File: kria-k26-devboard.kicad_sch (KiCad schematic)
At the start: 6 parts

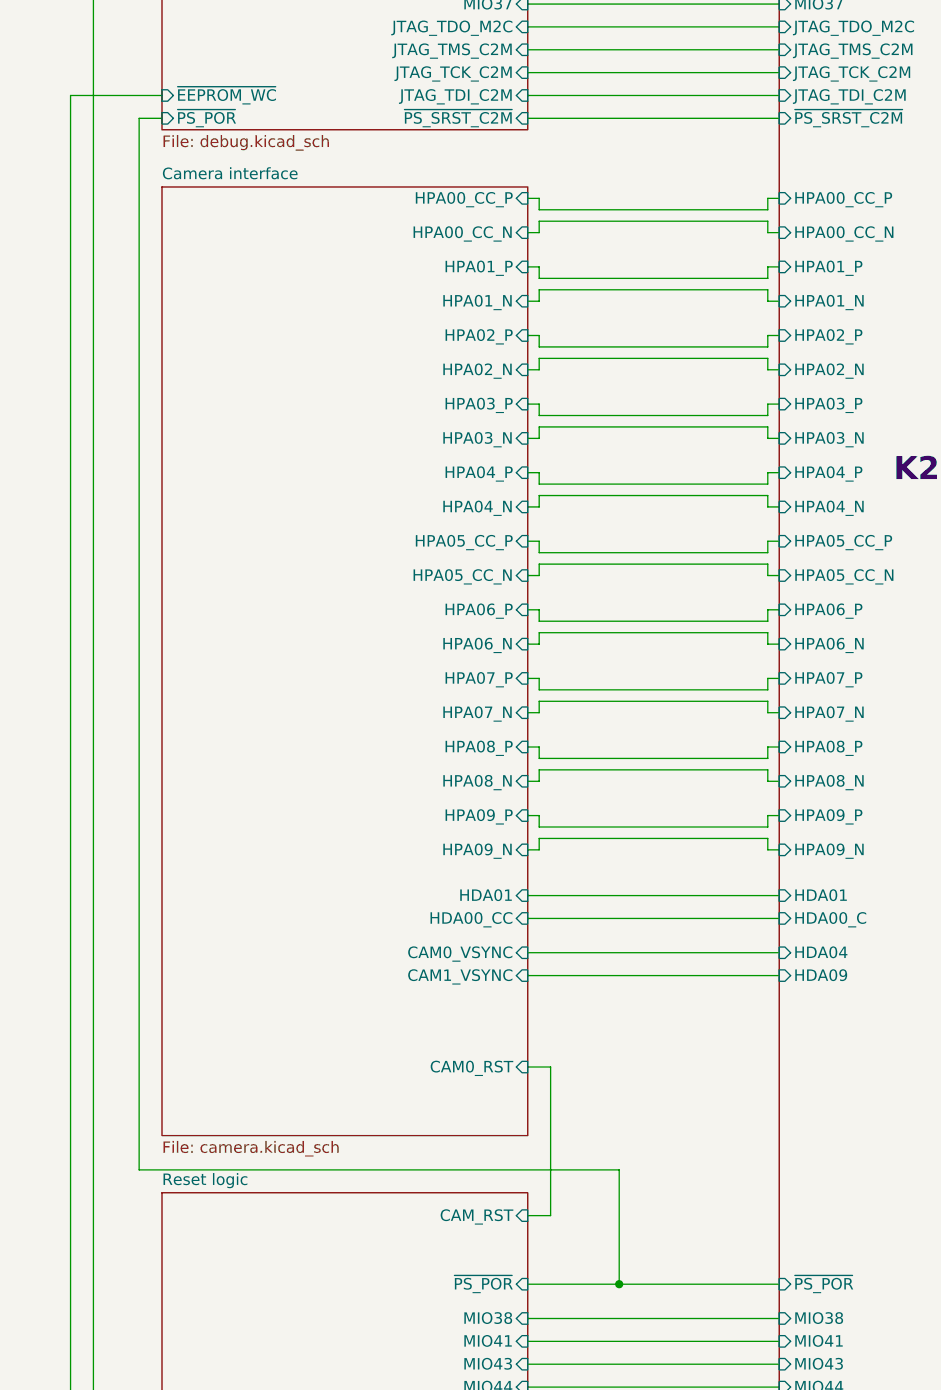
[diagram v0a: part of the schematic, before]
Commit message: Removed camera connector from schematic and pcb
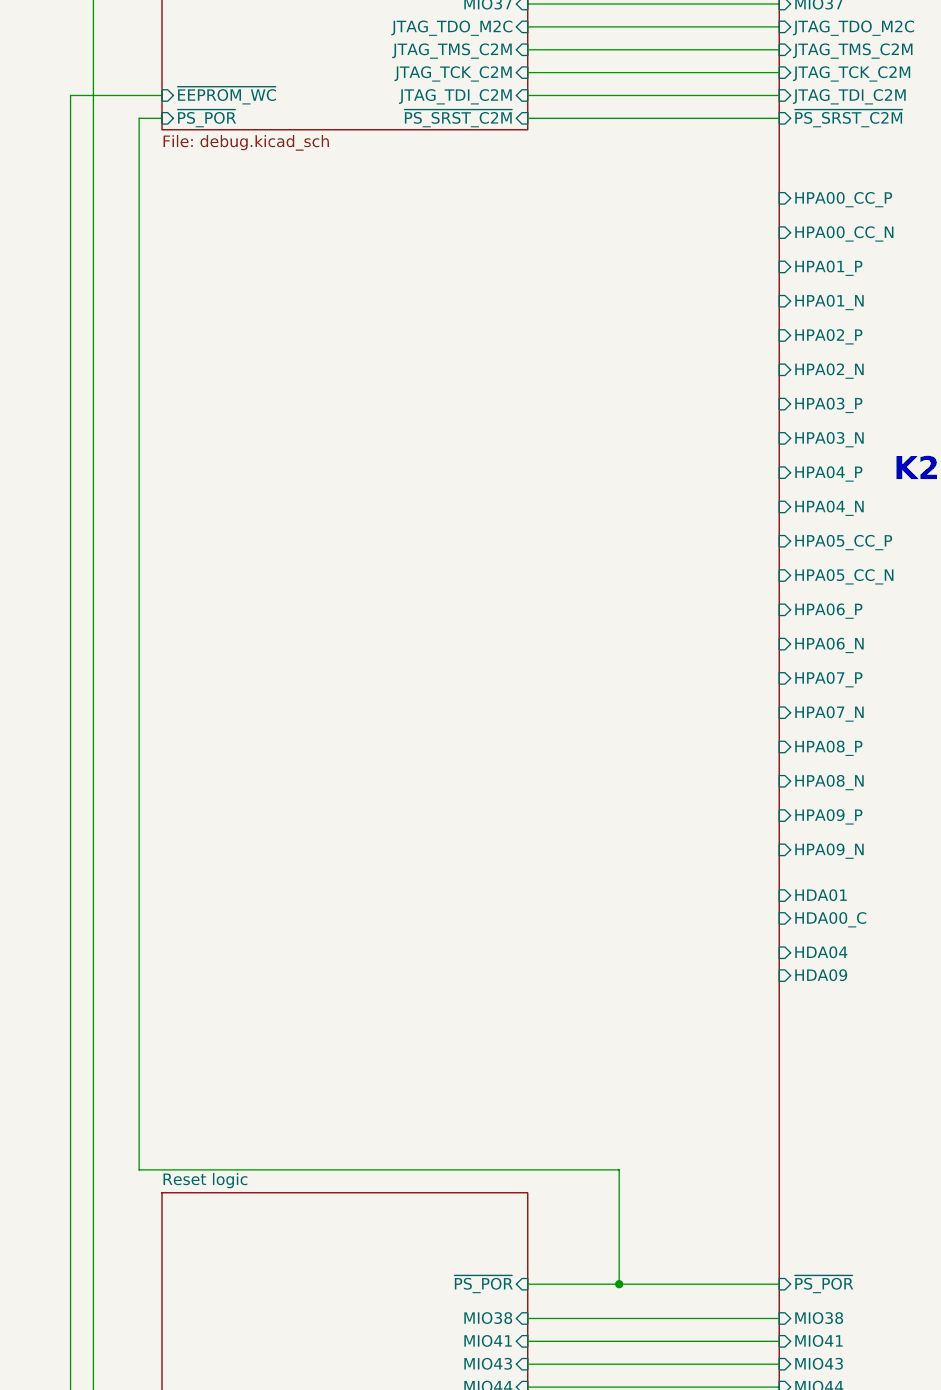
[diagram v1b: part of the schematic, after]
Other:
- removed sheet Camera interface
- sheet Reset logic ports: added none; removed CAM_RST

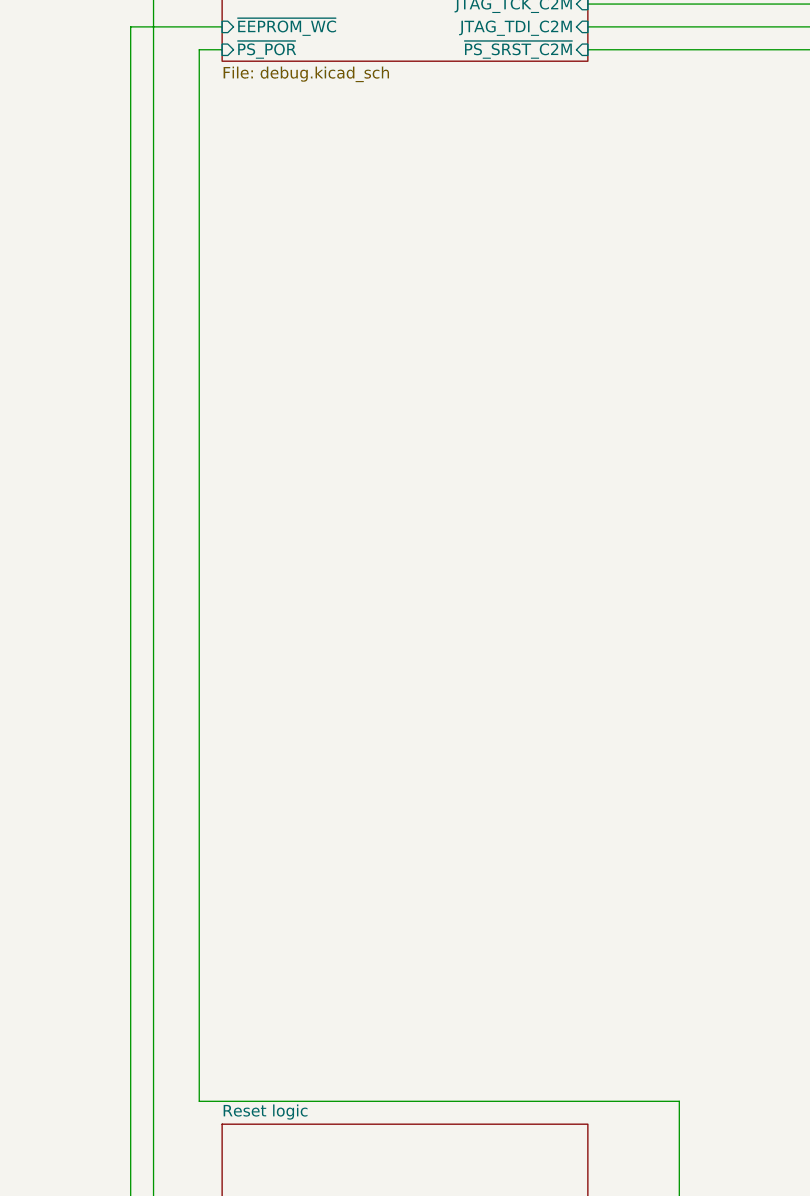
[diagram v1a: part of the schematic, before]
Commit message: Added radar board connector to project
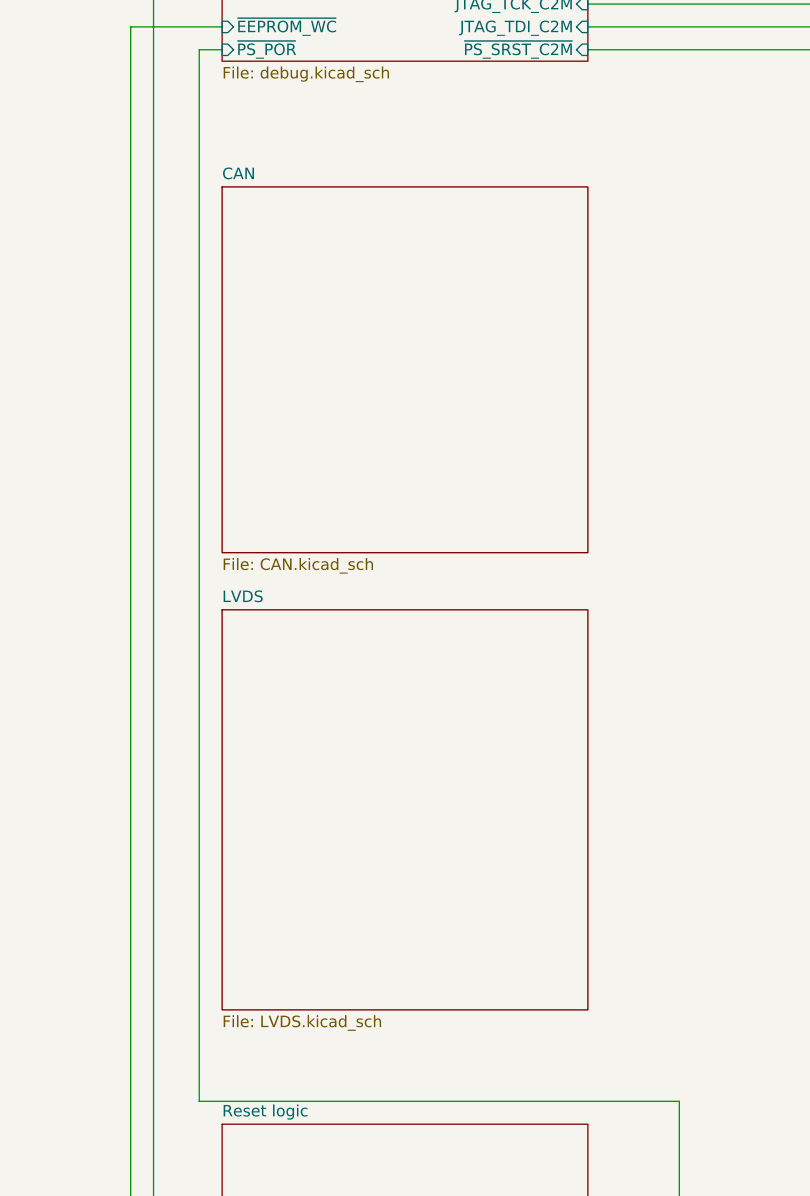
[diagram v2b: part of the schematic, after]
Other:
- added sheet CAN (CAN.kicad_sch)
- added sheet LVDS (LVDS.kicad_sch)
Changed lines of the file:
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@@
+		)
+	)
+	(sheet
+		(at 110.49 95.25)
+		(size 40.64 40.64)
+		(exclude_from_sim no)
+		(in_bom yes)
+		(on_board yes)
+		(dnp no)
+		(fields_autoplaced yes)
+		(stroke
+			(width 0.1524)
+			(type solid)
+		)
+		(fill
+			(color 0 0 0 0.0000)
+		)
+		(property "Sheetname" "CAN"
+			(at 110.49 94.5384 0)
+			(effects
+				(font
+					(size 1.27 1.27)
+				)
+				(justify left bottom)
+			)
+		)
+		(property "Sheetfile" "CAN.kicad_sch"
+			(at 110.49 136.4746 0)
+			(effects
+				(font
+					(size 1.27 1.27)
+				)
+				(justify left top)
+			)
+		)
+		(instances
+			(project "kria-k26-devboard"
+				(path "/c38c692d-dd84-4abf-ab35-63104b24d124"
+					(page "8")
+				)
+			)
+		)
+	)
+	(sheet
+		(at 110.49 142.24)
+		(size 40.64 44.45)
+		(exclude_from_sim no)
+		(in_bom yes)
+		(on_board yes)
+		(dnp no)
+		(fields_autoplaced yes)
+		(stroke
+			(width 0.1524)
+			(type solid)
+		)
+		(fill
+			(color 0 0 0 0.0000)
+		)
+		(property "Sheetname" "LVDS"
+			(at 110.49 141.5284 0)
+			(effects
+				(font
+					(size 1.27 1.27)
+				)
+				(justify left bottom)
+			)
+		)
+		(property "Sheetfile" "LVDS.kicad_sch"
+			(at 110.49 187.2746 0)
+			(effects
+				(font
+					(size 1.27 1.27)
+				)
+				(justify left top)
+			)
+		)
+		(instances
+			(project "kria-k26-devboard"
+				(path "/c38c692d-dd84-4abf-ab35-63104b24d124"
+					(page "9")
+				)
+			)
 		)
 	)

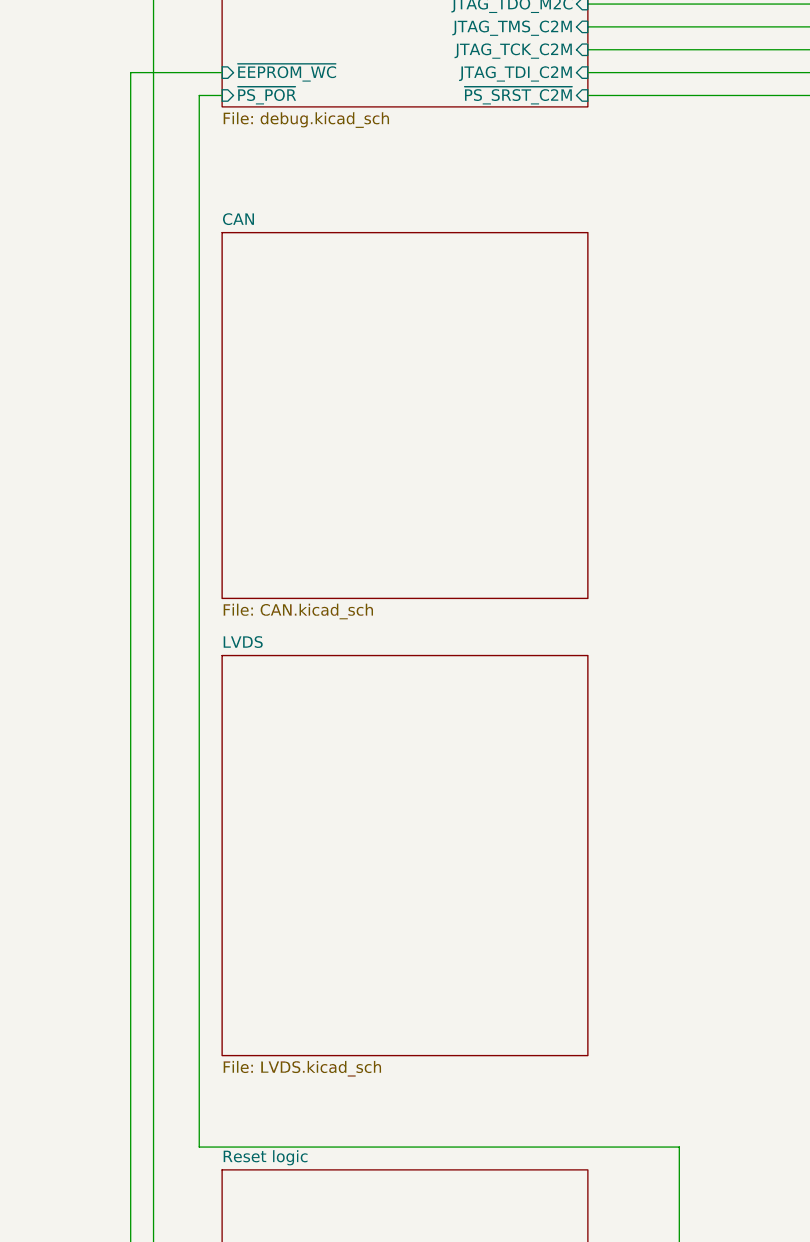
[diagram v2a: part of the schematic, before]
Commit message: Replaced LVDS connector with correct one and started pinning it out
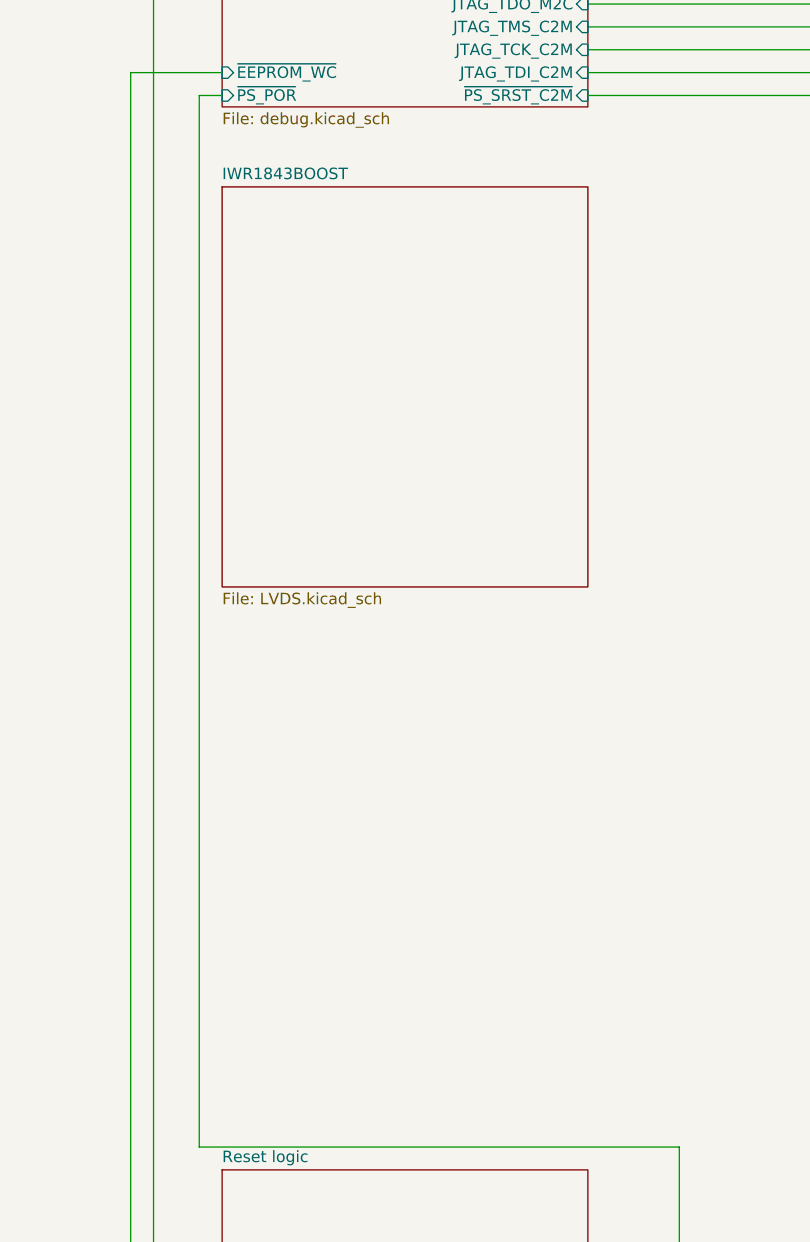
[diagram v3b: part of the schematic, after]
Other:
- sheet LVDS renamed IWR1843BOOST
- removed sheet CAN
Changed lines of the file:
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@@
 			(project "kria-k26-devboard"
 				(path "/c38c692d-dd84-4abf-ab35-63104b24d124"
-					(page "11")
+					(page "10")
 				)
 			)
@@
 			(project "kria-k26-devboard"
 				(path "/c38c692d-dd84-4abf-ab35-63104b24d124"
-					(page "16")
+					(page "15")
 				)
 			)
@@
 			(project "kria-k26-devboard"
 				(path "/c38c692d-dd84-4abf-ab35-63104b24d124"
-					(page "14")
+					(page "13")
 				)
 			)
@@
 			(project "kria-k26-devboard"
 				(path "/c38c692d-dd84-4abf-ab35-63104b24d124"
-					(page "18")
+					(page "17")
 				)
 			)
@@
 			(project "kria-k26-devboard"
 				(path "/c38c692d-dd84-4abf-ab35-63104b24d124"
-					(page "17")
+					(page "16")
 				)
 			)
@@
 			(project "kria-k26-devboard"
 				(path "/c38c692d-dd84-4abf-ab35-63104b24d124"
-					(page "12")
+					(page "11")
 				)
 			)
@@
 			(project "kria-k26-devboard"
 				(path "/c38c692d-dd84-4abf-ab35-63104b24d124"
-					(page "13")
+					(page "12")
 				)
 			)
@@
 			(project "kria-k26-devboard"
 				(path "/c38c692d-dd84-4abf-ab35-63104b24d124"
-					(page "15")
+					(page "14")
 				)
 			)
@@
 			(project "kria-k26-devboard"
 				(path "/c38c692d-dd84-4abf-ab35-63104b24d124"
-					(page "19")
+					(page "18")
 				)
 			)
@@
 			(project "kria-k26-devboard"
 				(path "/c38c692d-dd84-4abf-ab35-63104b24d124"
-					(page "10")
+					(page "9")
 				)
 			)
@@
 	)
 	(sheet
-		(at 110.49 95.25)
-		(size 40.64 40.64)
-		(exclude_from_sim no)
-		(in_bom yes)
-		(on_board yes)
-		(dnp no)
-		(fields_autoplaced yes)
-		(stroke
-			(width 0.1524)
-			(type solid)
-		)
-		(fill
-			(color 0 0 0 0.0000)
-		)
-		(property "Sheetname" "CAN"
-			(at 110.49 94.5384 0)
-			(effects
-				(font
-					(size 1.27 1.27)
-				)
-				(justify left bottom)
-			)
-		)
-		(property "Sheetfile" "CAN.kicad_sch"
-			(at 110.49 136.4746 0)
-			(effects
-				(font
-					(size 1.27 1.27)
-				)
-				(justify left top)
-			)
-		)
-		(instances
-			(project "kria-k26-devboard"
-				(path "/c38c692d-dd84-4abf-ab35-63104b24d124"
-					(page "8")
-				)
-			)
-		)
-	)
-	(sheet
-		(at 110.49 142.24)
+		(at 110.49 90.17)
 		(size 40.64 44.45)
 		(exclude_from_sim no)
@@
 			(color 0 0 0 0.0000)
 		)
-		(property "Sheetname" "LVDS"
-			(at 110.49 141.5284 0)
+		(property "Sheetname" "IWR1843BOOST"
+			(at 110.49 89.4584 0)
 			(effects
 				(font
@@
 		)
 		(property "Sheetfile" "LVDS.kicad_sch"
-			(at 110.49 187.2746 0)
+			(at 110.49 135.2046 0)
 			(effects
 				(font
@@
 			(project "kria-k26-devboard"
 				(path "/c38c692d-dd84-4abf-ab35-63104b24d124"
-					(page "9")
-				)
-			)
+					(page "8")
+				)
+			)
